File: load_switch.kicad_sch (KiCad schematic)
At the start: 5 parts, among them Q1 Q_Toshiba_SSM3J328R, Q2 Q_Toshiba_SSM3J328R

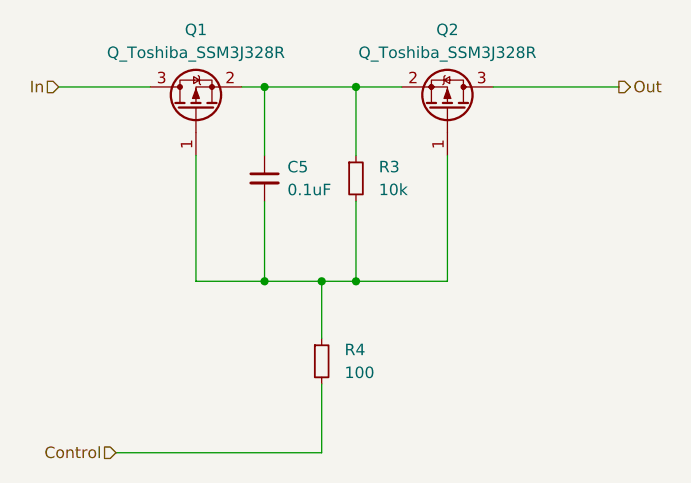
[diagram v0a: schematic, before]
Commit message: sch: add zener diode
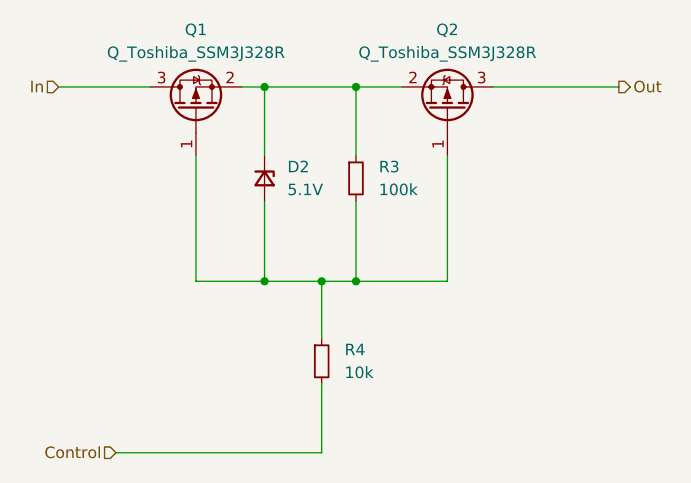
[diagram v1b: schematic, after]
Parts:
- removed C5: 0.1uF, Capacitor_SMD:C_0603_1608Metric, symbol Device:C_Small
- added D2: 5.1V, SOT:D_SOD-523, symbol Device:D_Zener_Small
- R3: value 10k -> 100k
- R4: value 100 -> 10k
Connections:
- net at Q1.2 (S), Q2.2 (S), R3.1: now also D2.1 (K)
- net at Q1.1 (G), Q2.1 (G), R3.2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: now also D2.2 (A)
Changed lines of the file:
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@@
-	)
-	(symbol
-		(lib_id "Device:C_Small")
-		(at 48.26 35.56 0)
-		(unit 1)
-		(exclude_from_sim no)
-		(in_bom yes)
-		(on_board yes)
-		(dnp no)
-		(fields_autoplaced yes)
-		(property "Reference" "C5"
-			(at 50.8 34.2962 0)
-			(effects
-				(font
-					(size 1.27 1.27)
-				)
-				(justify left)
-			)
-		)
-		(property "Value" "0.1uF"
-			(at 50.8 36.8362 0)
-			(effects
-				(font
-					(size 1.27 1.27)
-				)
-				(justify left)
-			)
-		)
-		(property "Footprint" "Capacitor_SMD:C_0603_1608Metric"
-			(at 48.26 35.56 0)
-			(effects
-				(font
-					(size 1.27 1.27)
-				)
-				(hide yes)
-			)
-		)
-		(property "Datasheet" "~"
-			(at 48.26 35.56 0)
-			(effects
-				(font
-					(size 1.27 1.27)
-				)
-				(hide yes)
-			)
-		)
-		(property "Description" "Unpolarized capacitor, small symbol"
-			(at 48.26 35.56 0)
-			(effects
-				(font
-					(size 1.27 1.27)
-				)
-				(hide yes)
-			)
-		)
-		(pin "2"
-		)
-		(pin "1"
-		)
-		(instances
-			(project "project-hw-usbc-mux-demux"
-				(path "/a3c0ab3f-ca32-4edb-a5c1-d200028ec7dc/4e455b7c-bdd8-4869-96e6-828b850a961d"
-					(reference "C5")
-					(unit 1)
-				)
-			)
-		)
 	)
 	(symbol
@@
 			)
 		)
-		(property "Value" "100"
+		(property "Value" "10k"
 			(at 57.15 57.1499 0)
 			(effects
@@
 			)
 		)
-		(property "Value" "10k"
+		(property "Value" "100k"
 			(at 60.96 36.8299 0)
 			(effects
@@
 					(unit 1)
 				)
+			)
+		)
+	)
+	(symbol
+		(lib_id "Device:D_Zener_Small")
+		(at 48.26 35.56 270)
+		(unit 1)
+		(exclude_from_sim no)
+		(in_bom yes)
+		(on_board yes)
+		(dnp no)
+		(fields_autoplaced yes)
+		(property "Reference" "D2"
+			(at 50.8 34.2899 90)
+			(effects
+				(font
+					(size 1.27 1.27)
+				)
+				(justify left)
+			)
+		)
+		(property "Value" "5.1V"
+			(at 50.8 36.8299 90)
+			(effects
+				(font
+					(size 1.27 1.27)
+				)
+				(justify left)
+			)
+		)
+		(property "Footprint" "SOT:D_SOD-523"
+			(at 48.26 35.56 90)
+			(effects
+				(font
+					(size 1.27 1.27)
+				)
+				(hide yes)
+			)
+		)
+		(property "Datasheet" "~"
+			(at 48.26 35.56 90)
+			(effects
+				(font
+					(size 1.27 1.27)
+				)
+				(hide yes)
+			)
+		)
+		(property "Description" "Zener diode, small symbol"
+			(at 48.26 35.56 0)
+			(effects
+				(font
+					(size 1.27 1.27)
+				)
+				(hide yes)
+			)
+		)
+		(pin "2"
+		)
+		(pin "1"
+		)
+		(instances
+			(project ""
+				(path "/a3c0ab3f-ca32-4edb-a5c1-d200028ec7dc/4e455b7c-bdd8-4869-96e6-828b850a961d"
+					(reference "D2")
+					(unit 1)
+				)
